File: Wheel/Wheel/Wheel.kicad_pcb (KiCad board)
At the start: 2 copper layers, 162 x 112 mm, 124 parts, among them J1 Conn_02x09_Odd_Even, J10 RJ45, J11 Screw_Terminal_01x02, J12 DS-201, J13 Conn_01x04, J14 Conn_02x13_Top_Bottom, J15 DB25_Female, J16 Conn_01x06, J17 Conn_01x07, J18 Conn_01x06, J19 RJ45, J2 RJ45, J20 DB9_Male, J21 DB9_Female, J3 RJ45, J4 RJ45, J5 USB_B, J6 Conn_02x10_Odd_Even, J7 Conn_02x09_Odd_Even, J8 RJ45, J9 RJ45, U1 MCP23S17_SP, U10 PC817, U11 IP4220CZ6, U12 PC817, U13 IP4220CZ6, U2 STM32F407VETx, U3 MCP23S17_SP, U4 USBLC6-2SC6, U5 AMS1117, U6 4N35, U7 PC817, U8 PC817, U9 PC817, Y1 32,768 кГц, Y2 8MHz

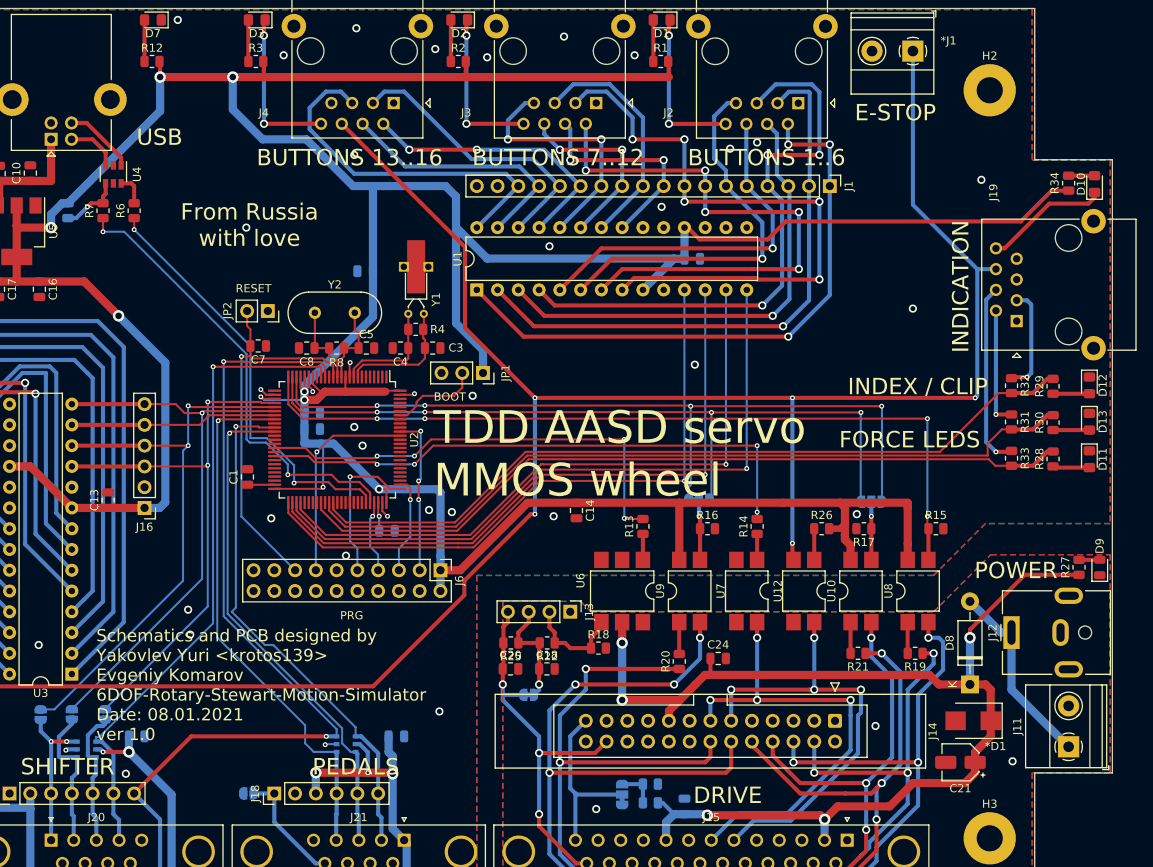
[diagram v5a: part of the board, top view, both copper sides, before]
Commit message: I've added a connector for connect STM32F407G-DISK1 to the Wheel board
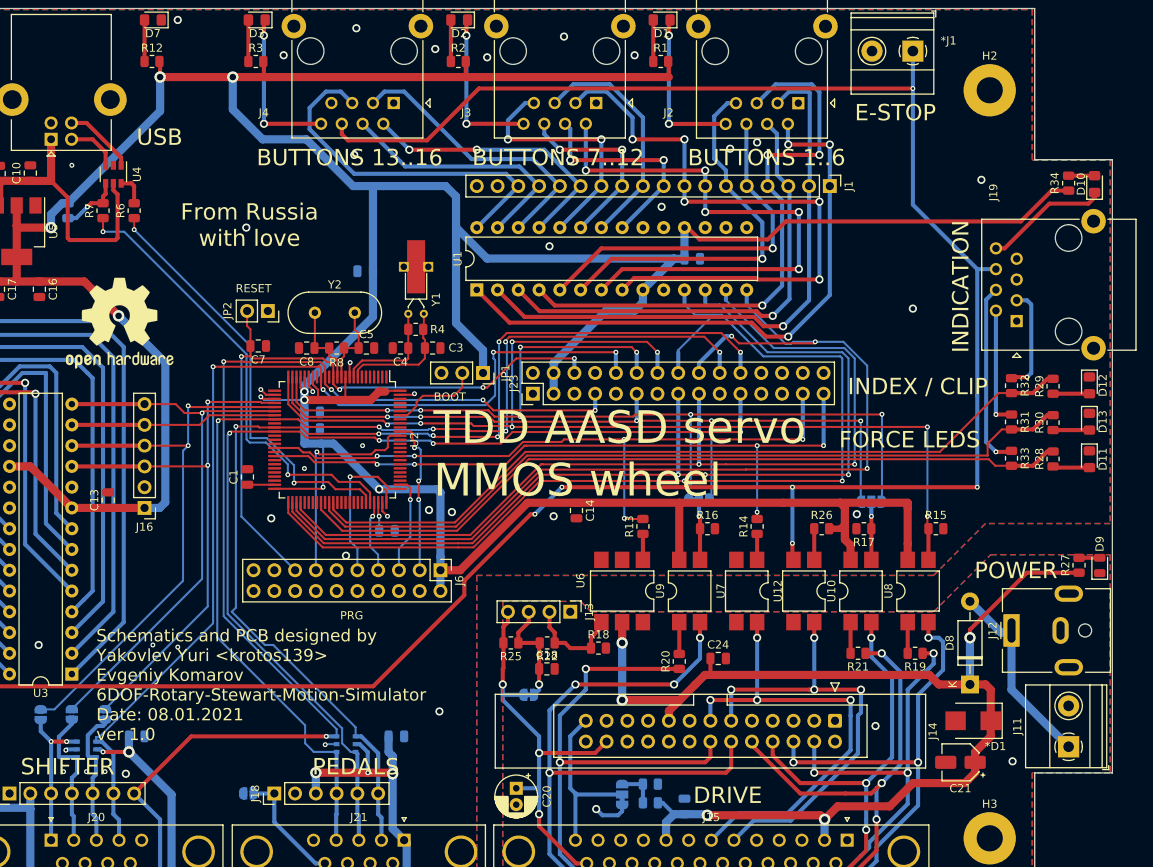
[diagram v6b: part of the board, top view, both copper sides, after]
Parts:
- added J23: Conn_02x15_Odd_Even, Connector_PinHeader_2.54mm:PinHeader_2x15_P2.54mm_Vertical, F.Cu at (121.2, 71.1)
- added LOGO1: Logo_Open_Hardware_Large, Symbol:OSHW-Logo2_14.6x12mm_SilkScreen, F.Cu at (70.6, 62.5)
- C20: footprint Capacitor_SMD:C_0805_2012Metric -> Capacitor_THT:CP_Radial_D5.0mm_P2.00mm
- R27: value 560 -> 1k
- moved C20 14.6 mm to (119.1, 119.4), turned to 270 degrees
- moved J12 0.25 mm to (179.7, 100.1)
- moved R27 0.25 mm to (188.0, 92.1)
- moved D9 0.25 mm to (190.5, 92.1)
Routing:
- net PEDAL_GAS: track 64.8 -> 137.8 mm, vias 1 -> 6
- net PEDAL_CLUCH: track 66.1 -> 136.0 mm, vias 1 -> 6
- net PEDAL_BREAK: track 62.7 -> 125.6 mm, vias 1 -> 4
- net SHIFTER_X: track 80.1 -> 127.2 mm, vias 1 -> 4
- net CS: track 78.2 -> 121.9 mm, vias 1 -> 2
- net SO: track 82.9 -> 125.5 mm, vias 1 -> 3
- net SCK: track 79.3 -> 120.2 mm, vias 1 -> 3
- net SHIFTER_Y: track 113.9 -> 151.1 mm, vias 4 -> 7
- net SI: track 79.1 -> 115.1 mm, vias 1 -> 2
- net RESET: track 47.7 -> 81.7 mm, vias 1 -> 4
- net ENC_I: track 99.6 -> 130.4 mm, vias 4 -> 7
- net DRV_PWM: track 56.2 -> 83.6 mm, vias 4 -> 5
- net ENC_A: track 98.4 -> 122.3 mm, vias 4 -> 7
- net 5V: track 14.5 -> 35.5 mm
- net 3V: track 738.4 -> 759.1 mm
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
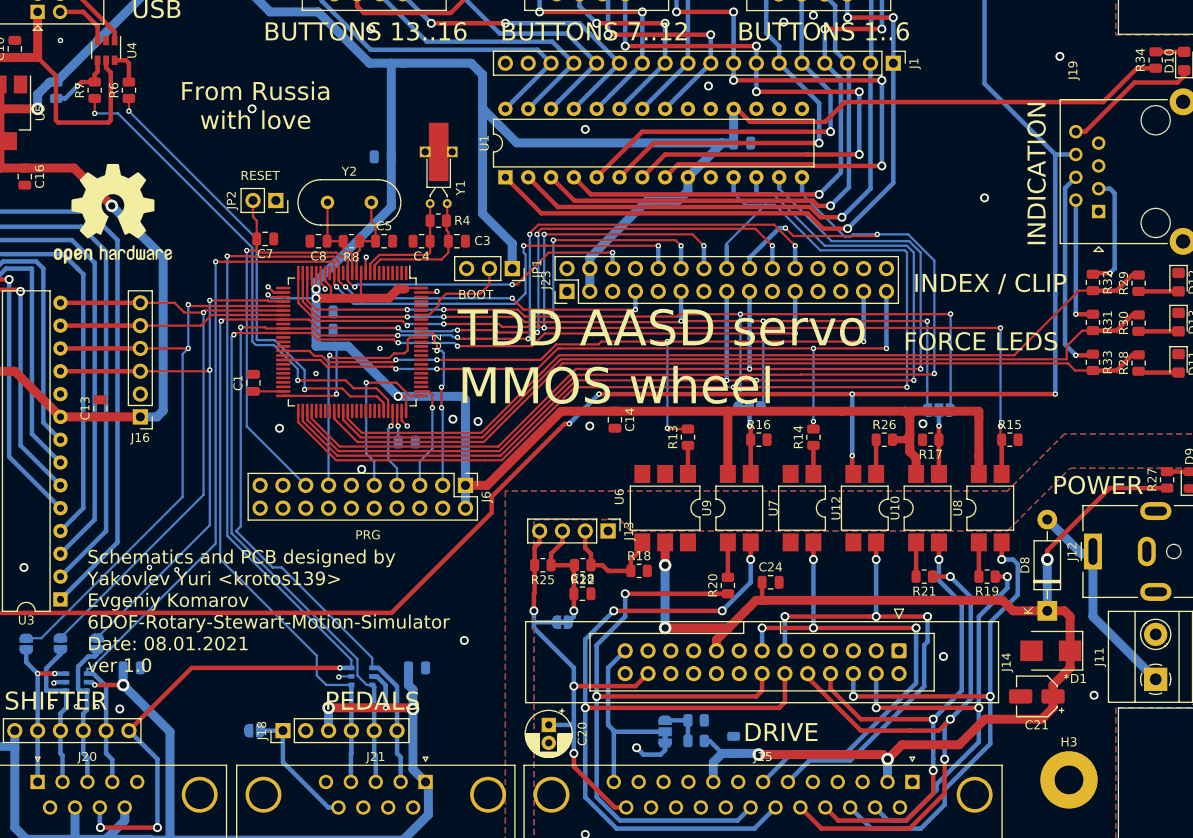
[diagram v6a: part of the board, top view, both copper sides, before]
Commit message: Wheel's scheme updated
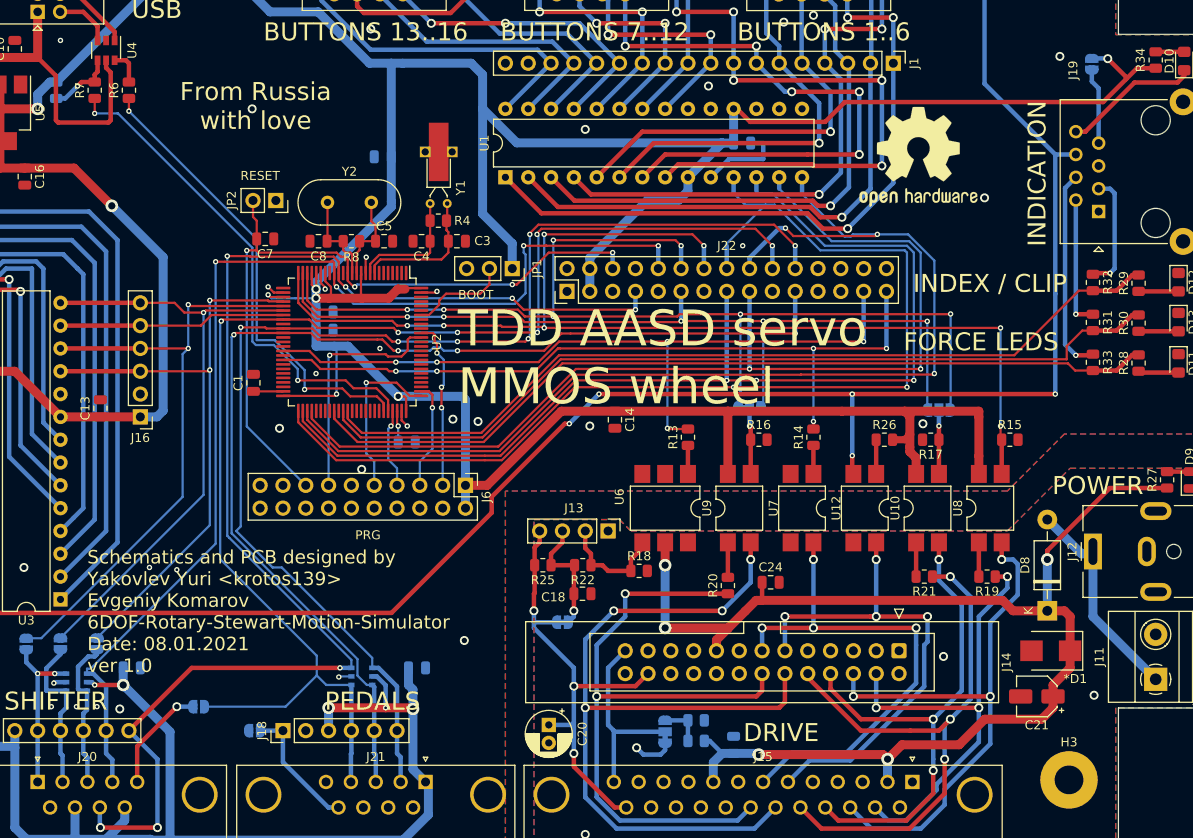
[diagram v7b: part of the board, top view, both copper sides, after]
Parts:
- added JP11: SolderJumper_2_Open, Jumper:SolderJumper-2_P1.3mm_Open_RoundedPad1.0x1.5mm, B.Cu at (179.6, 45.8)
- added JP12: SolderJumper_2_Open, Jumper:SolderJumper-2_P1.3mm_Open_RoundedPad1.0x1.5mm, B.Cu at (80.2, 117.3)
- R18: value 1K -> 2K
- moved LOGO1 89.9 mm to (160.3, 56.1)
- renumbered J23 to J22
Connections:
- J19 pad 7: (no net) -> Net-(J19-Pad7)
- J20 pad 5: (no net) -> Net-(J20-Pad5)
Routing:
- net PEDAL_CLUCH: track 136.0 -> 149.8 mm
- net Net-(J20-Pad5): track 0.00 -> 12.0 mm, vias 0 -> 1
- net GND: track 12.3 -> 22.2 mm, vias 45 -> 46
- net Net-(J19-Pad7): track 0.00 -> 8.44 mm
- net 3V: track 759.1 -> 764.0 mm, vias 17 -> 18
- net /B7: track 69.0 -> 67.2 mm
- net PEDAL_BREAK: track 125.6 -> 126.4 mm

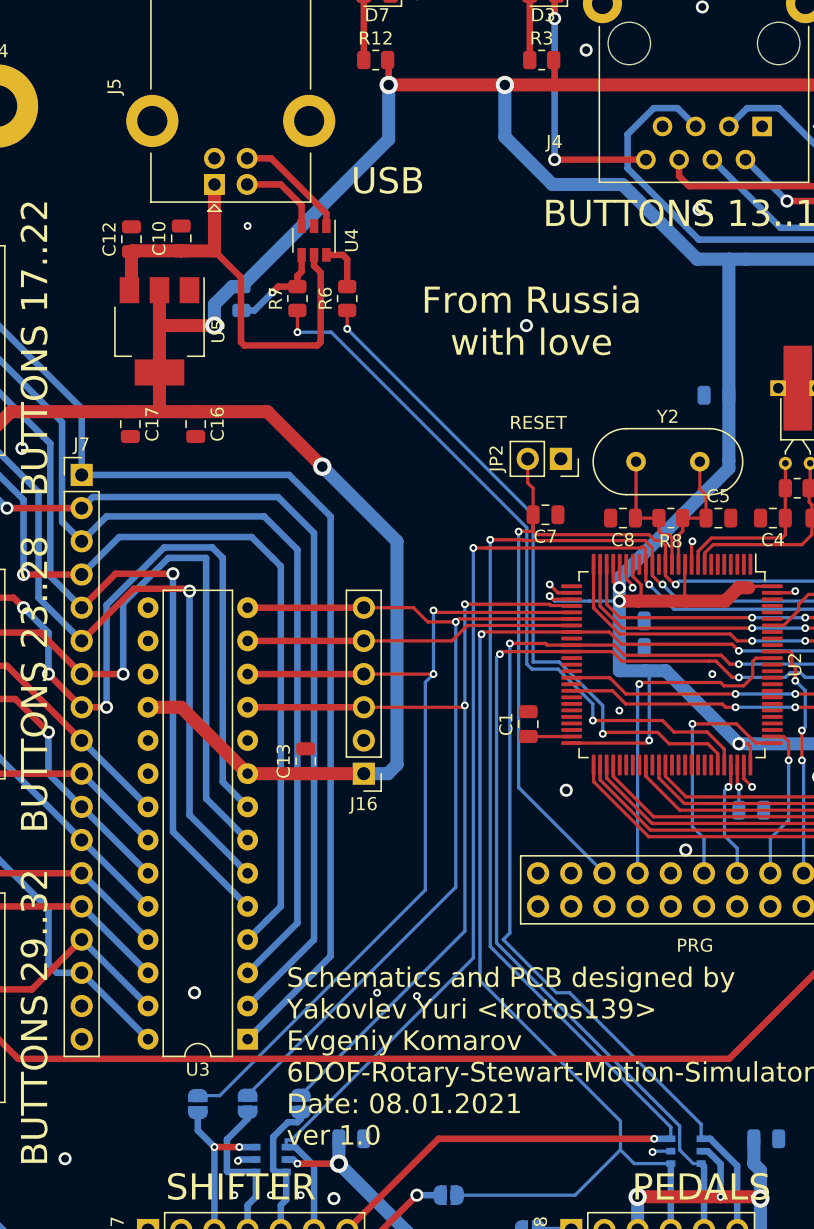
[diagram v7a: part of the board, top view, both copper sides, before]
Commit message: I've added rear button for logitech h shifter
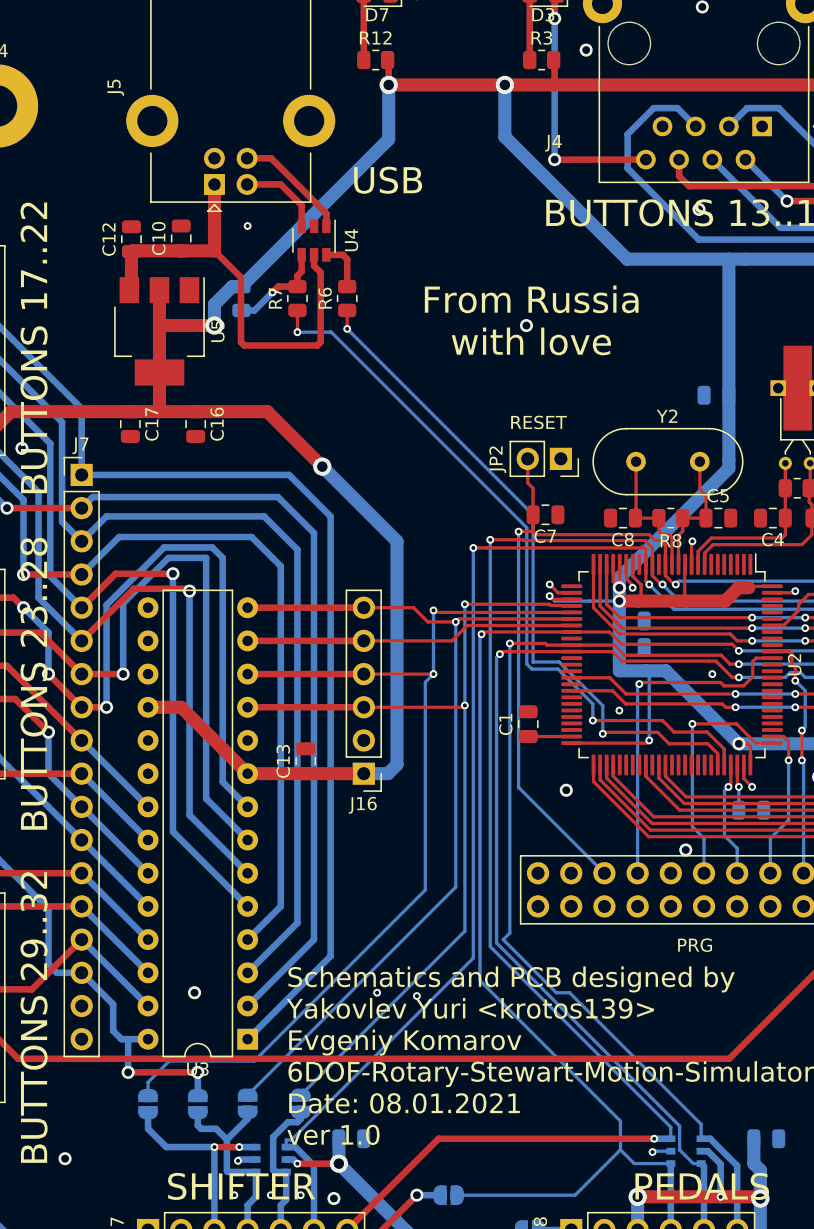
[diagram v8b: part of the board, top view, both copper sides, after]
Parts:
- added JP12: SolderJumper_2_Open, Jumper:SolderJumper-2_P1.3mm_Open_RoundedPad1.0x1.5mm, B.Cu at (61.0, 110.4)
- moved JP9 3.81 mm to (57.1, 110.4)
- renumbered JP12 to JP13
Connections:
- net /B32 renamed SHIFTER_REAR
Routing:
- net SHIFTER_REAR: track 35.5 -> 46.4 mm, vias 0 -> 2
- net SPI1_SCK: track 70.4 -> 74.8 mm
- net SPI1_SCK_PROT: track 18.4 -> 22.1 mm
- net SPI1_SO_PROT: track 17.9 -> 21.6 mm
